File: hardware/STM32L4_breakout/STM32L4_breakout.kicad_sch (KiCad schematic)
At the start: 66 parts, among them J1 12V IN, J10 GPIO, J12 USART1, J13 USART3, J15 3.3V, J16 5V, J17 12V, J2 SWD, J3 Conn_01x08, J4 Conn_01x06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

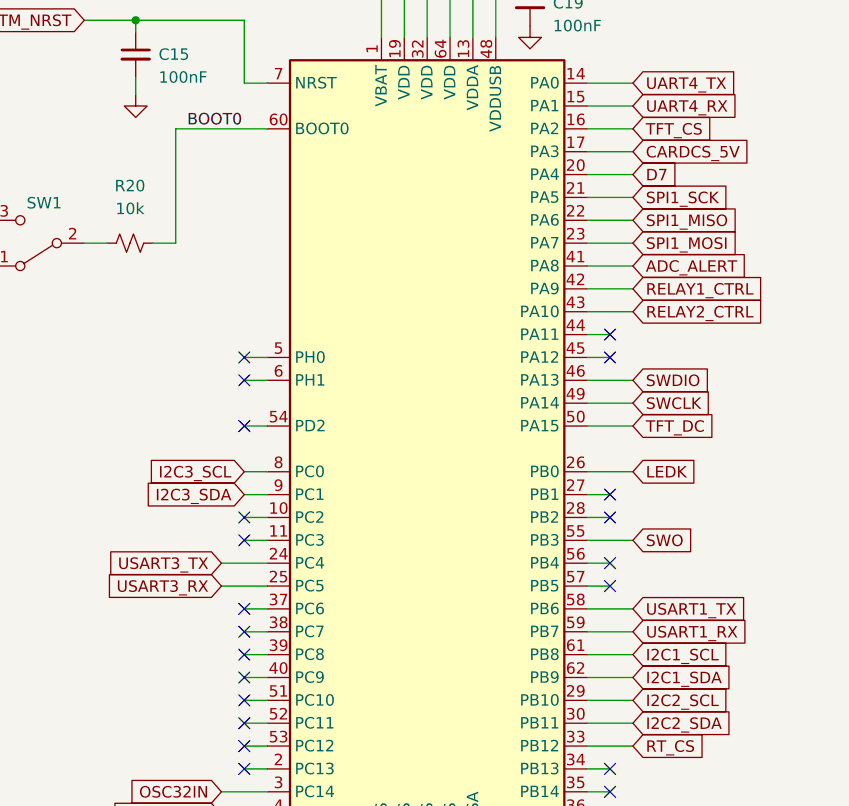
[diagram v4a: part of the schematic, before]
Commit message: breakout board re-routed D7
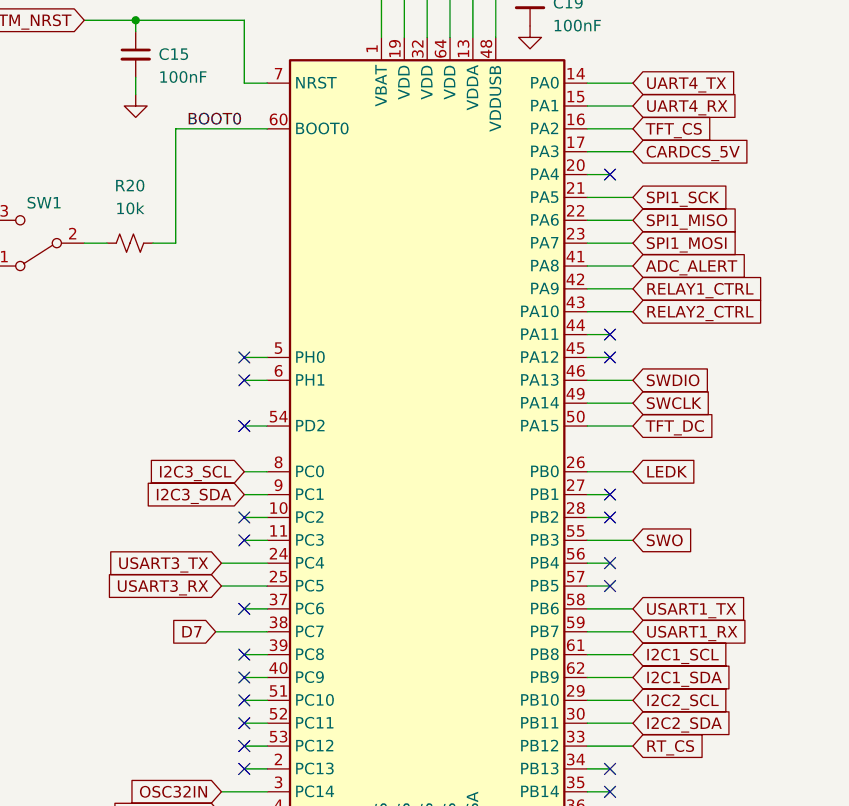
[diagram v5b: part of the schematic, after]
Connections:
- net D7: now also U4.38 (PC7); no longer U4.20 (PA4)
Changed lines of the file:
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@@
   (no_connect (at 209.55 107.95))
   (no_connect (at 209.55 128.27))
-  (no_connect (at 168.91 113.03))
+  (no_connect (at 168.91 118.11))
   (no_connect (at 24.13 178.435))
   (no_connect (at 62.865 180.975))
@@
   (no_connect (at 209.55 130.81))
   (no_connect (at 168.91 123.19))
+  (no_connect (at 209.55 62.23))
   (no_connect (at 209.55 105.41))
   (no_connect (at 209.55 100.33))
@@
   (no_connect (at 209.55 133.35))
   (no_connect (at 24.13 186.055))
-  (no_connect (at 168.91 118.11))
   (no_connect (at 168.91 110.49))
   (polyline (pts (xy 127 19.05) (xy 127 144.78))
@@
     (stroke (width 0) (type default) (color 0 0 0 0))
   )
+  (wire (pts (xy 209.55 62.23) (xy 207.01 62.23))
+    (stroke (width 0) (type default) (color 0 0 0 0))
+  )
   (wire (pts (xy 43.815 150.495) (xy 24.13 150.495))
     (stroke (width 0) (type default) (color 0 0 0 0))
@@
     (stroke (width 0) (type default) (color 0 0 0 0))
   )
+  (wire (pts (xy 165.735 113.03) (xy 171.45 113.03))
+    (stroke (width 0) (type default) (color 0 0 0 0))
+  )
   (wire (pts (xy 207.01 64.77) (xy 212.09 64.77))
     (stroke (width 0) (type default) (color 0 0 0 0))
   )
+  (wire (pts (xy 168.91 118.11) (xy 171.45 118.11))
+    (stroke (width 0) (type default) (color 0 0 0 0))
+  )
   (wire (pts (xy 207.01 67.31) (xy 212.09 67.31))
     (stroke (width 0) (type default) (color 0 0 0 0))
@@
     (stroke (width 0) (type default) (color 0 0 0 0))
   )
-  (wire (pts (xy 168.91 113.03) (xy 171.45 113.03))
-    (stroke (width 0) (type default) (color 0 0 0 0))
-  )
   (wire (pts (xy 256.54 109.22) (xy 256.54 106.68))
     (stroke (width 0) (type default) (color 0 0 0 0))
@@
     (stroke (width 0) (type default) (color 0 0 0 0))
   )
-  (wire (pts (xy 168.91 118.11) (xy 171.45 118.11))
-    (stroke (width 0) (type default) (color 0 0 0 0))
-  )
   (wire (pts (xy 62.865 145.415) (xy 81.915 145.415))
     (stroke (width 0) (type default) (color 0 0 0 0))
@@
   )
   (wire (pts (xy 100.965 53.975) (xy 100.965 66.675))
-    (stroke (width 0) (type default) (color 0 0 0 0))
-  )
-  (wire (pts (xy 207.01 62.23) (xy 212.09 62.23))
     (stroke (width 0) (type default) (color 0 0 0 0))
   )
@@
     )
   )
-  (global_label "D7" (shape input) (at 212.09 62.23 0) (fields_autoplaced)
-    (effects (font (size 1.27 1.27)) (justify left))
-    (property "Intersheet References" "${INTERSHEET_REFS}" (id 0) (at 216.9826 62.1506 0)
-      (effects (font (size 1.27 1.27)) (justify left) hide)
-    )
-  )
+  (global_label "D7" (shape input) (at 165.735 113.03 180) (fields_autoplaced)
+    (effects (font (size 1.27 1.27)) (justify right))
+    (property "Intersheet References" "${INTERSHEET_REFS}" (id 0) (at 160.8424 112.9506 0)
+      (effects (font (size 1.27 1.27)) (justify right) hide)
+    )
+  )

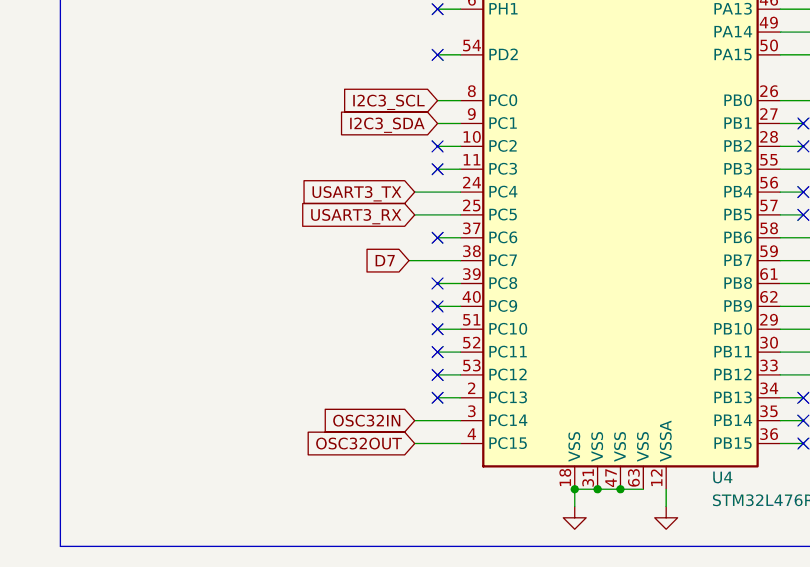
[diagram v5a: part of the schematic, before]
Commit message: d7 change to schematic
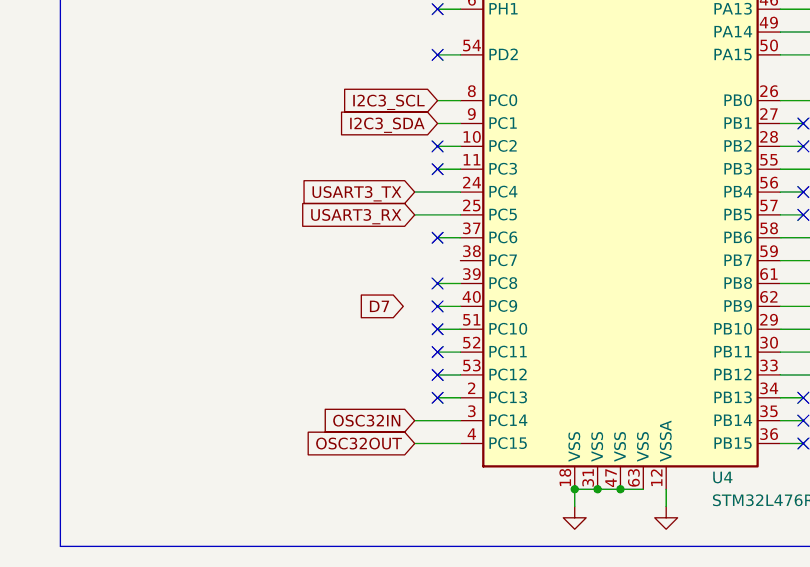
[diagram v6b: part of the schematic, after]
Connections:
- net D7: no longer U4.38 (PC7)
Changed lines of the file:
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@@
-    (stroke (width 0) (type default) (color 0 0 0 0))
-  )
-  (wire (pts (xy 165.735 113.03) (xy 171.45 113.03))
     (stroke (width 0) (type default) (color 0 0 0 0))
   )
@@
     )
   )
-  (global_label "D7" (shape input) (at 165.735 113.03 180) (fields_autoplaced)
-    (effects (font (size 1.27 1.27)) (justify right))
-    (property "Intersheet References" "${INTERSHEET_REFS}" (id 0) (at 160.8424 112.9506 0)
-      (effects (font (size 1.27 1.27)) (justify right) hide)
-    )
+  (global_label "D7" (shape input) (at 165.1 118.11 180) (fields_autoplaced)
+    (effects (font (size 1.27 1.27)) (justify right))
+    (property "Intersheet References" "${INTERSHEET_REFS}" (id 0) (at 160.2074 118.0306 0)
+      (effects (font (size 1.27 1.27)) (justify right) hide)
+    )

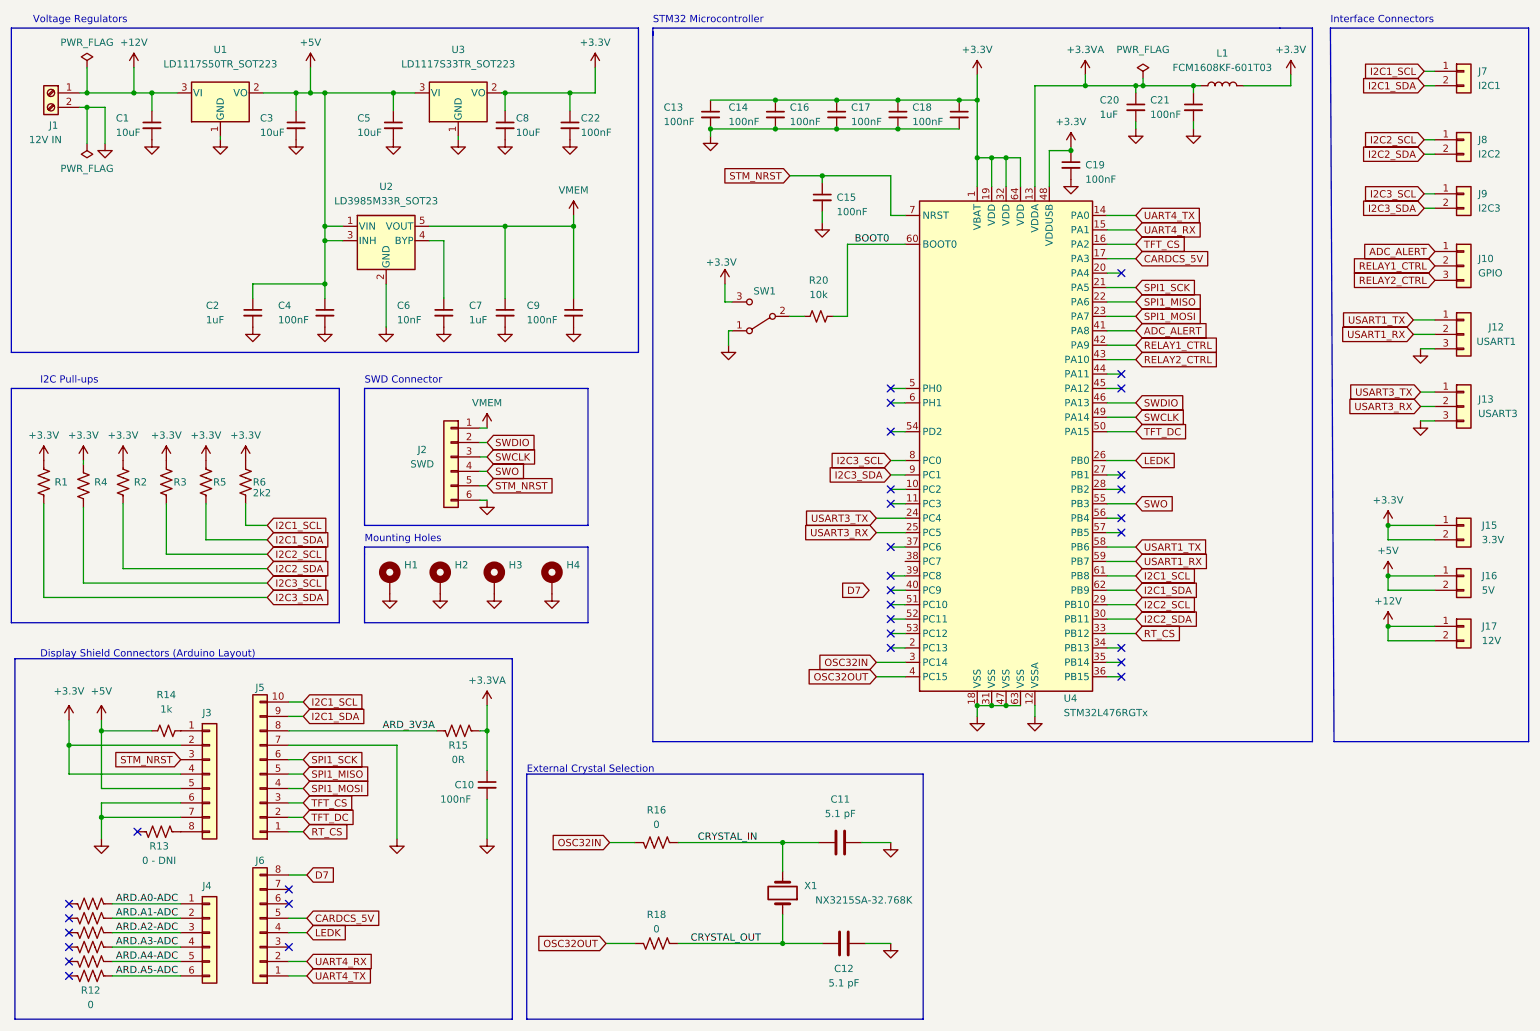
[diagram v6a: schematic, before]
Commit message: added pwr indicator LEDs
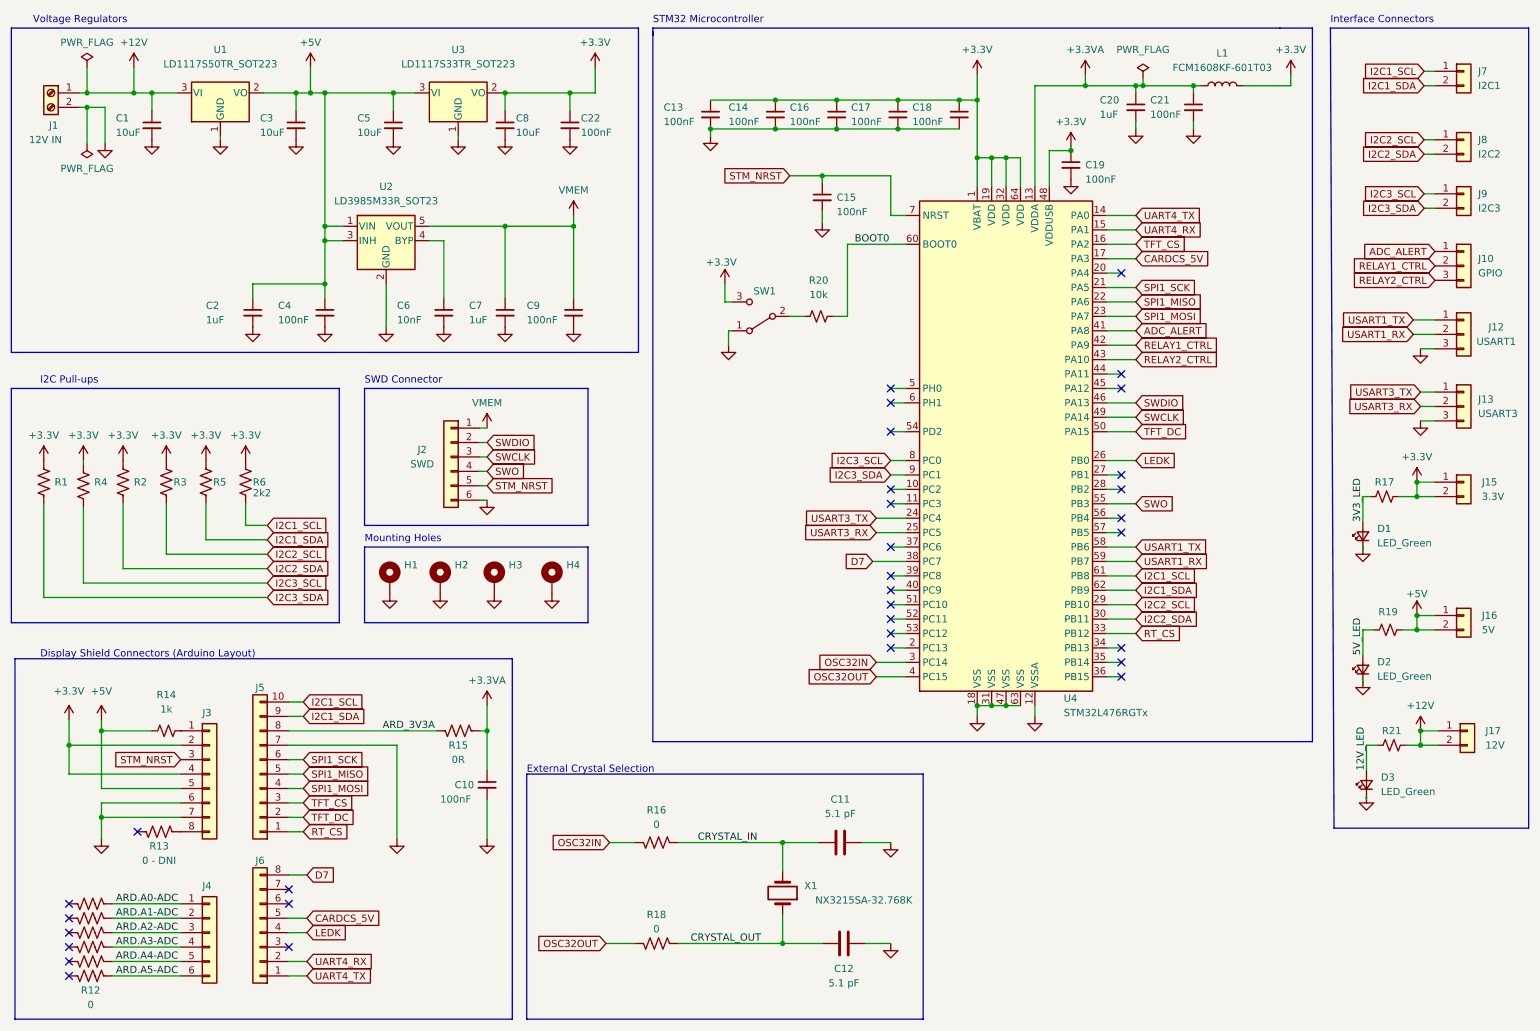
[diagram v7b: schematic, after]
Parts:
- added D1, D2, D3: LED_Green, LED_SMD:LED_0603_1608Metric, symbol Device:LED_Small
- added R17, R19, R21: 330R, Resistor_SMD:R_0603_1608Metric, symbol Device:R_Small_US
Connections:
- net +12V: now also R21.2
- net +3.3V: now also R17.2
- net +5V: now also R19.2
- net D7: now also U4.38 (PC7)
- net GND: now also D1.1 (K), D2.1 (K), D3.1 (K)
- new net 12V_LED: D3.2 (A), R21.1
- new net 3V3_LED: D1.2 (A), R17.1
- new net 5V_LED: D2.2 (A), R19.1
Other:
- moved on the sheet: J15, J16, J17

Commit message: breakout board power routing WIP
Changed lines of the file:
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@@
     (stroke (width 0) (type default) (color 0 0 0 0))
   )
-  (wire (pts (xy 137.16 36.83) (xy 137.16 38.1))
+  (wire (pts (xy 137.16 36.83) (xy 137.16 39.37))
     (stroke (width 0) (type default) (color 0 0 0 0))
   )
@@
     (pin "8")
   )
-  (symbol (lib_id "power:GND") (at 137.16 38.1 0) (unit 1)
+  (symbol (lib_id "power:GND") (at 137.16 39.37 0) (unit 1)
     (in_bom yes) (on_board yes) (fields_autoplaced)
-    (property "Reference" "#PWR030" (id 0) (at 137.16 44.45 0)
+    (property "Reference" "#PWR030" (id 0) (at 137.16 45.72 0)
       (effects (font (size 1.27 1.27)) hide)
     )
-    (property "Value" "GND" (id 1) (at 137.16 43.18 0)
+    (property "Value" "GND" (id 1) (at 137.16 44.45 0)
       (effects (font (size 1.27 1.27)) hide)
     )
-    (property "Footprint" "" (id 2) (at 137.16 38.1 0)
+    (property "Footprint" "" (id 2) (at 137.16 39.37 0)
       (effects (font (size 1.27 1.27)) hide)
     )
-    (property "Datasheet" "" (id 3) (at 137.16 38.1 0)
+    (property "Datasheet" "" (id 3) (at 137.16 39.37 0)
       (effects (font (size 1.27 1.27)) hide)
     )
